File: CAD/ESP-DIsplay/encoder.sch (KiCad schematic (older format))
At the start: 4 parts, among them SW501 Encoder

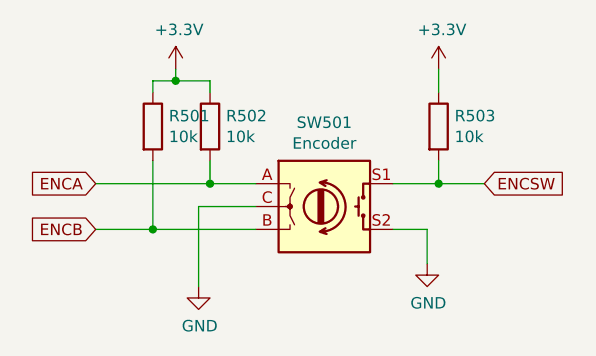
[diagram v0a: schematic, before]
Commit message: esp12e adc pinsadded, 1117 power module
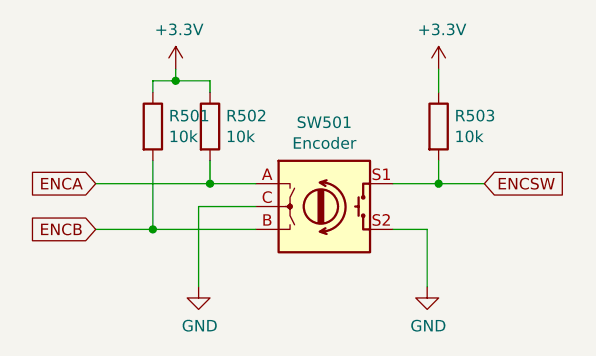
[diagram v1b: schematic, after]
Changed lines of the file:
@@
 L power:GND #PWR?
 U 1 1 60C79811
-P 6150 4300
+P 6150 4400
 AR Path="/60C79811" Ref="#PWR?"  Part="1"
 AR Path="/60C58A4D/60C5A69E/60C79811" Ref="#PWR0503"  Part="1"
-F 0 "#PWR0503" H 6150 4050 50  0001 C CNN
-F 1 "GND" H 6155 4127 50  0000 C CNN
-F 2 "" H 6150 4300 50  0001 C CNN
-F 3 "" H 6150 4300 50  0001 C CNN
-	1    6150 4300
+F 0 "#PWR0503" H 6150 4150 50  0001 C CNN
+F 1 "GND" H 6155 4227 50  0000 C CNN
+F 2 "" H 6150 4400 50  0001 C CNN
+F 3 "" H 6150 4400 50  0001 C CNN
+	1    6150 4400
 	1    0    0    -1
 $EndComp
@@
 Wire Wire Line
 	5150 4050 5150 4400
-Wire Wire Line
-	6150 4150 6150 4300
 Wire Wire Line
 	6000 4150 6150 4150
@@
 	1    0    0    -1
 $EndComp
+Wire Wire Line
+	6150 4150 6150 4400
 $EndSCHEMATC

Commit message: ESP32 added
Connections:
- net ENCA renamed TDN
- net ENCB renamed TUP
- net ENCSW renamed TON
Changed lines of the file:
@@
 $Descr A4 11693 8268
 encoding utf-8
-Sheet 5 8
+Sheet 6 9
 Title ""
 Date ""
@@
 Wire Wire Line
 	6200 3450 6200 3550
-Text GLabel 4700 3950 0    50   Input ~ 0
-ENCA
-Text GLabel 4700 4150 0    50   Input ~ 0
-ENCB
-Text GLabel 6400 3950 2    50   Input ~ 0
-ENCSW
 Wire Wire Line
 	6200 3950 6400 3950
@@
 Wire Wire Line
 	6150 4150 6150 4400
+Text GLabel 6400 3950 2    50   Input ~ 0
+TON
+Text GLabel 4700 3950 0    50   Input ~ 0
+TDN
+Text GLabel 4700 4150 0    50   Input ~ 0
+TUP
 $EndSCHEMATC
